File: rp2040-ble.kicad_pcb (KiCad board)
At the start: 2 copper layers, 75 x 62 mm, 41 parts, among them J1 Conn_01x15, J2 Conn_01x15, J3 USB_B_Micro, J4 Conn_01x03, SW1 PTS810_SJK_250_SMTR_LFS, SW2 PTS810_SJK_250_SMTR_LFS, U1 RP2040, U2 W25Q128JVS, U3 HM-BT4502, U4 NCP1117DT33G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

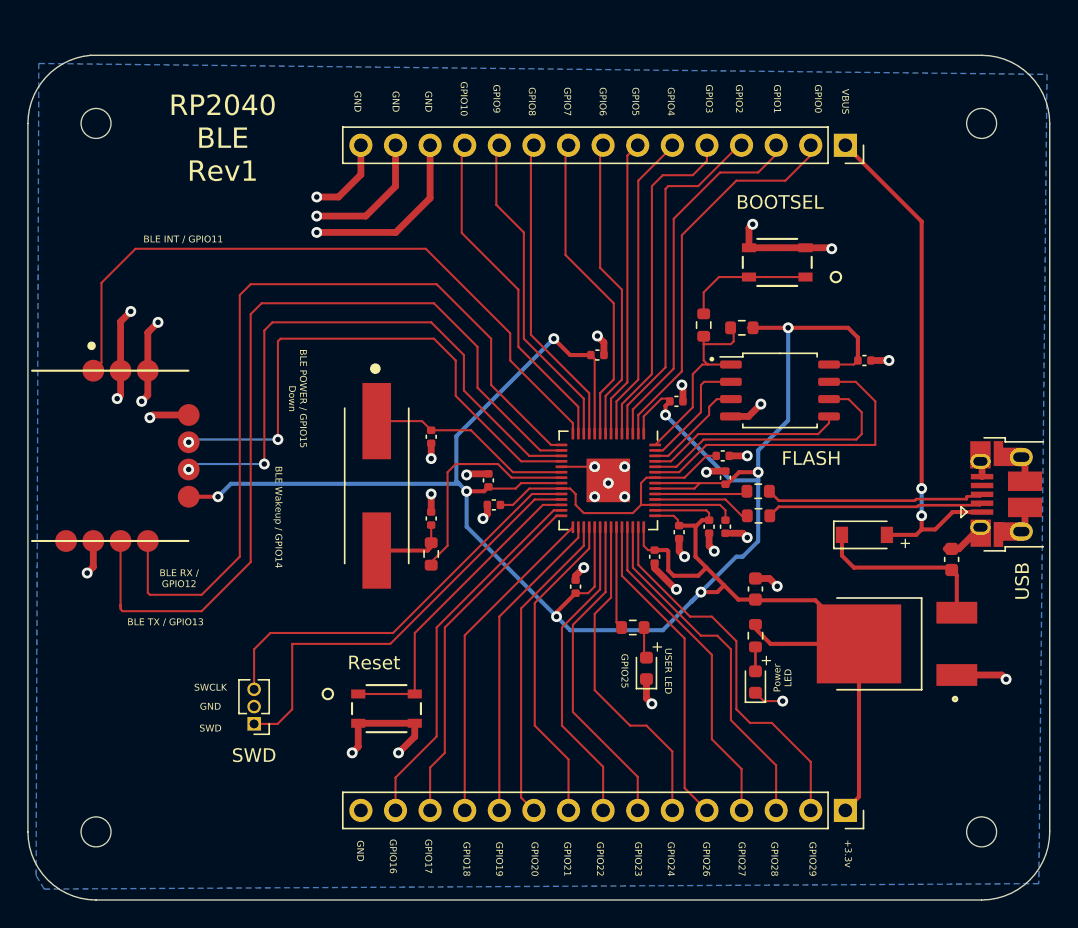
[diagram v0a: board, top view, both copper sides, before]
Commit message: Incorporate review feedback
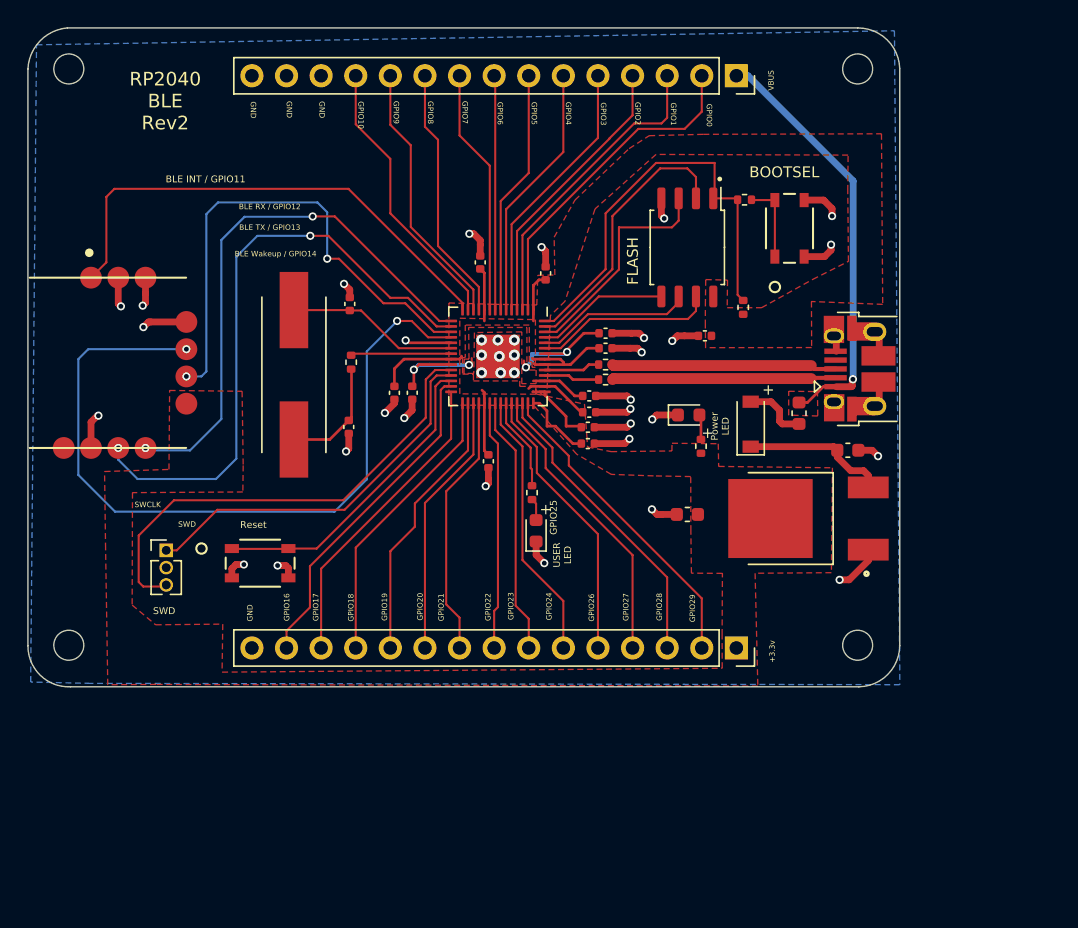
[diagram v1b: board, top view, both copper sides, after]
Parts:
- added F1: 100mA, Fuse:Fuse_0603_1608Metric, F.Cu at (146.6, 93.3)
- R1, R2, R4, R5, R6, R7, R8: footprint Resistor_SMD:R_0603_1608Metric -> Resistor_SMD:R_0402_1005Metric
- moved H2 67.8 mm to (150.9, 110.3)
- moved H3 67.1 mm to (93.0, 68.0)
- moved H1 56.7 mm to (150.9, 68.0)
- moved D2 20.2 mm to (138.5, 93.4), turned to 0 degrees
- moved R4 15.3 mm to (113.7, 89.5), turned to -90 degrees
- moved R2 15.0 mm to (132.4, 90.8)
- moved R1 14.6 mm to (132.4, 89.7)
- moved R7 14.5 mm to (139.4, 95.7), turned to 90 degrees
- moved J2 14.4 mm to (142.0, 110.5)
- moved J4 14.3 mm to (100.2, 103.3), turned to 0 degrees
- moved J3 14.2 mm to (151.0, 90.0)
- moved SW2 14.1 mm to (107.0, 104.3)
- moved C8 13.9 mm to (131.2, 92.0), turned to 0 degrees
- moved H4 13.8 mm to (93.0, 110.3)
- moved C1 13.4 mm to (128.0, 83.0), turned to 90 degrees
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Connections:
- D3 pad 2: /VBUS -> Net-(D3-Pad2)
- J1 pad 1: /VBUS -> VBUS
- J3 pad 1: /VBUS -> VBUS
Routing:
- net +3.3V: track 201.3 -> 42.5 mm, vias 8 -> 0
- net GND: track 109.3 -> 68.4 mm, vias 37 -> 38
- net /VBUS: track 38.2 -> 0.00 mm, vias 2 -> 0
- net VBUS: track 0.00 -> 31.3 mm, vias 0 -> 1
- net /BLE_RX: track 61.8 -> 40.4 mm, vias 0 -> 2
- net /BLE_TX: track 63.8 -> 44.7 mm, vias 0 -> 2
- net /BLE_POWER_DOWN: track 40.0 -> 57.0 mm
- net /QSPI_SS: track 14.9 -> 31.7 mm
- net /BLE_INT: track 49.6 -> 36.7 mm
- net /QSPI_SD1: track 8.82 -> 20.0 mm
- net /QSPI_SD3: track 24.2 -> 13.3 mm
- net /QSPI_SCLK: track 20.6 -> 11.5 mm
- net /QSPI_SD2: track 7.64 -> 16.7 mm
- net /XOUT: track 16.1 -> 7.39 mm
- net /GPIO6: track 23.1 -> 17.2 mm
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- added copper zone on F.Cu, net +1V1
- added copper zone on F.Cu, net +3.3V
- added copper zone on F.Cu, net VBUS
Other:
- board size 75 x 62 mm -> 64 x 48.4 mm
- board text added: "RP2040 BLE Rev2"
- board text removed: "BLE POWER / GPIO15 Down"
- board text removed: "RP2040 BLE Rev1"
- board text removed: "USB"

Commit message: Generate board screenshots
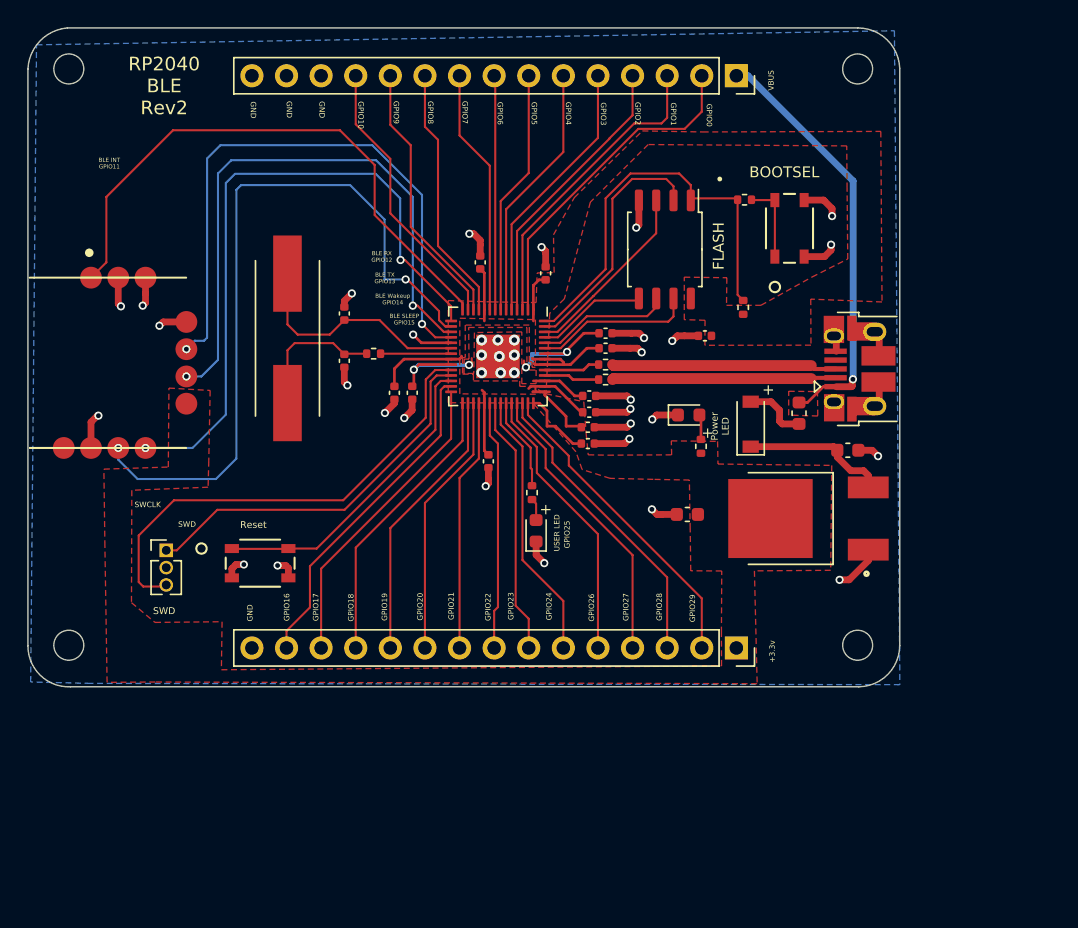
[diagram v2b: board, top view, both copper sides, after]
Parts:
- moved C13 4.87 mm to (113.2, 89.4)
- moved Y1 2.72 mm to (109.0, 87.8)
- moved R4 1.76 mm to (115.4, 88.9), turned to 180 degrees
- moved U2 1.66 mm to (136.8, 81.2)
- moved C10 0.81 mm to (113.2, 86.0)
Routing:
- net /BLE_POWER_DOWN: track 57.0 -> 44.7 mm
- net /BLE_TX: track 44.7 -> 53.6 mm
- net /BLE_RX: track 40.4 -> 48.4 mm
- net /BLE_WAKEUP: track 37.4 -> 43.9 mm
- net /BLE_INT: track 36.7 -> 42.5 mm
- net /XIN: track 12.7 -> 17.3 mm
- net /QSPI_SD2: track 16.7 -> 13.6 mm
- net /XOUT: track 7.39 -> 5.18 mm
- net /QSPI_SD1: track 20.0 -> 18.2 mm
- net Net-(C13-Pad1): track 8.52 -> 10.3 mm
- net /QSPI_SD0: track 9.80 -> 8.09 mm
- net /QSPI_SCLK: track 11.5 -> 9.90 mm
- net /QSPI_SD3: track 13.3 -> 11.7 mm
- net GND: track 68.4 -> 67.4 mm
- net /GPIO21: track 19.4 -> 18.6 mm
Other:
- board text added: "BLE INT GPIO11"
- board text added: "BLE RX GPIO12"
- board text added: "BLE SLEEP GPIO15"
- board text added: "BLE TX GPIO13"
- board text added: "BLE Wakeup GPIO14"
- board text removed: "BLE INT / GPIO11"
- board text removed: "BLE RX / GPIO12"
- board text removed: "BLE TX / GPIO13"
- board text removed: "BLE Wakeup / GPIO14"
